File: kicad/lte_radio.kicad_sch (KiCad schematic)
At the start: 24 parts, among them J11 JAE_SIM_Card_SF72S006, J13 Conn_01x06, J14 Conn_01x06, Q1 2N7002, U24 MONARCH_2_GM02S, U26 TXB0108DQSR

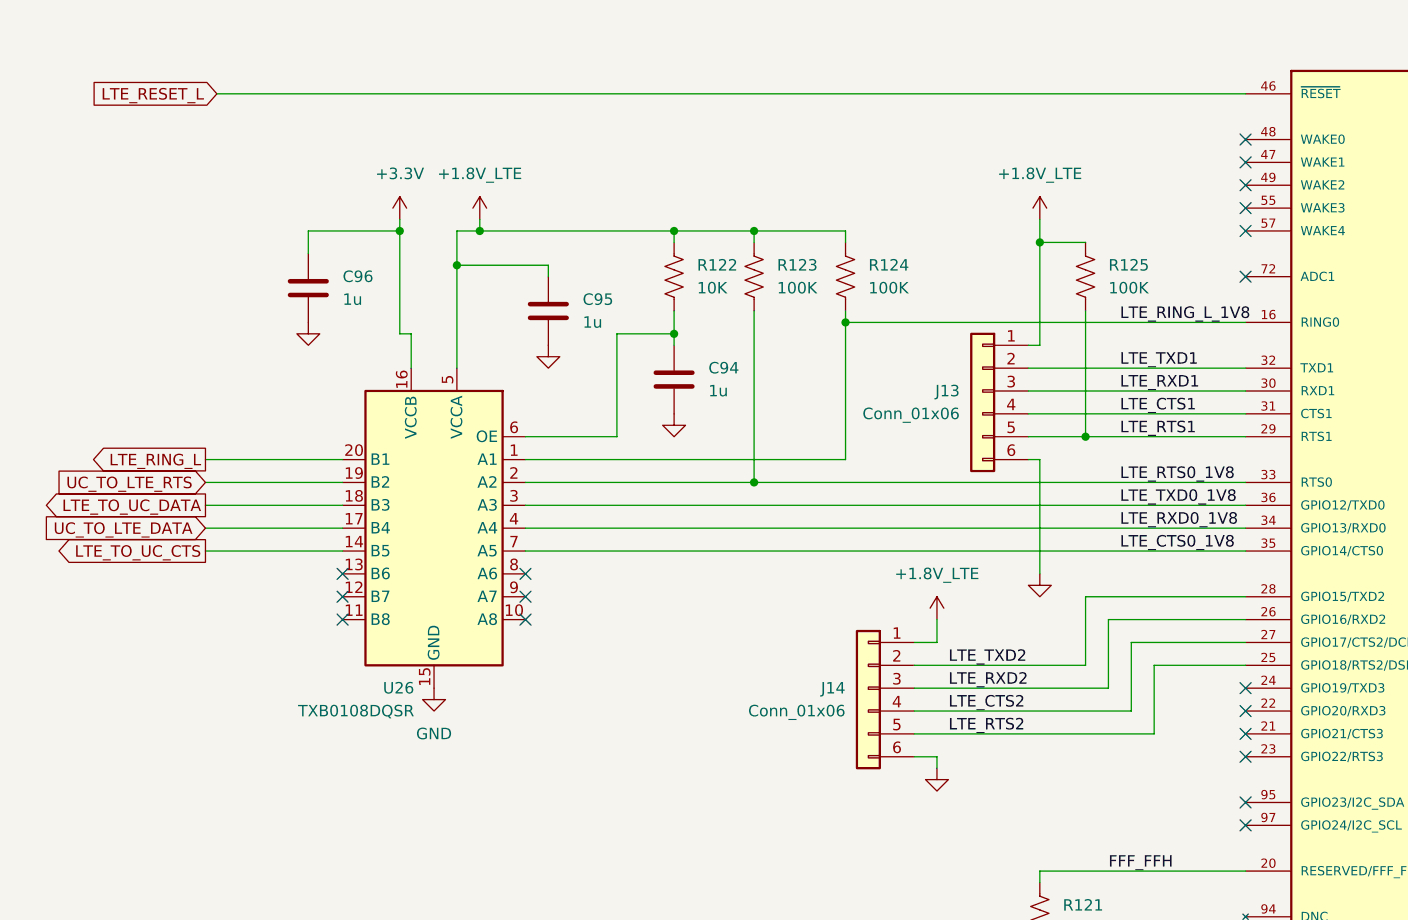
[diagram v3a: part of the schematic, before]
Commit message: swap txb0108 package, fix pin 65 on cpld
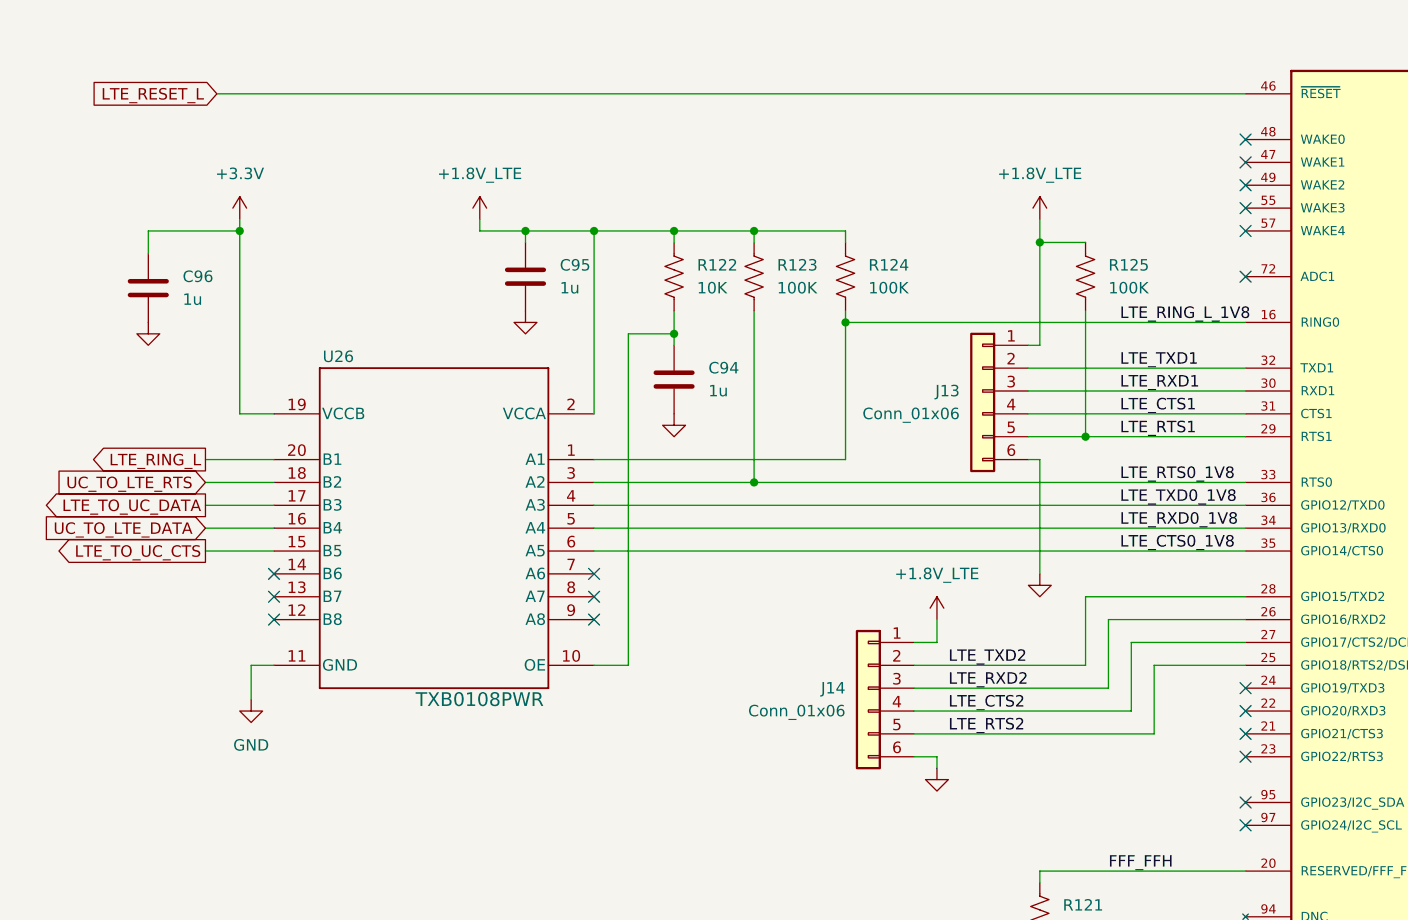
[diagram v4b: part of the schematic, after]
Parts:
- U26: value TXB0108DQSR -> TXB0108PWR; footprint Package_SON:USON-20_2x4mm_P0.4mm -> bgelb_footprint:PW0020A_N; symbol Logic_LevelTranslator:TXB0108DQSR -> bgelb_lib:TXB0108PWR
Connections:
- net +3.3V: now also U26.19 (VCCB), U26.2 (VCCA); no longer U26.16 (VCCB), U26.5 (VCCA)
- net GND: now also U26.11 (GND); no longer U26.15 (GND)
- net LTE_CTS0_1V8: now also U26.6 (A5); no longer U26.7 (A5)
- net LTE_RTS0_1V8: now also U26.3 (A2); no longer U26.2 (A2)
- net LTE_RXD0_1V8: now also U26.5 (A4); no longer U26.4 (A4)
- net LTE_TO_UC_CTS: now also U26.15 (B5); no longer U26.14 (B5)
- net LTE_TO_UC_DATA: now also U26.17 (B3); no longer U26.18 (B3)
- net LTE_TXD0_1V8: now also U26.4 (A3); no longer U26.3 (A3)
- net UC_TO_LTE_DATA: now also U26.16 (B4); no longer U26.17 (B4)
- net UC_TO_LTE_RTS: now also U26.18 (B2); no longer U26.19 (B2)
- net at U26.10 (OE): now also C94.1, R122.2
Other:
- moved on the sheet: C95, C96

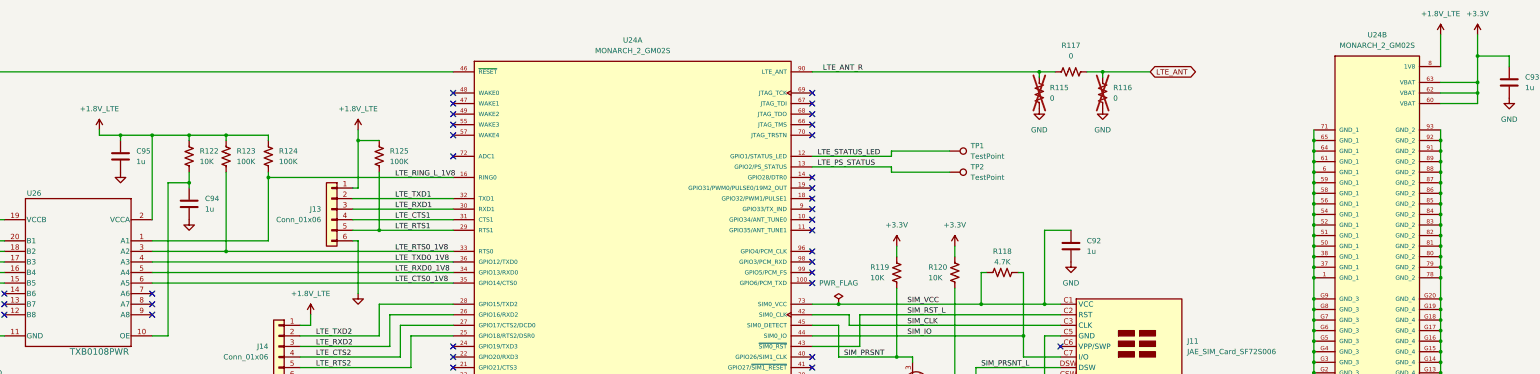
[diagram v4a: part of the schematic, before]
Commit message: kicad version update
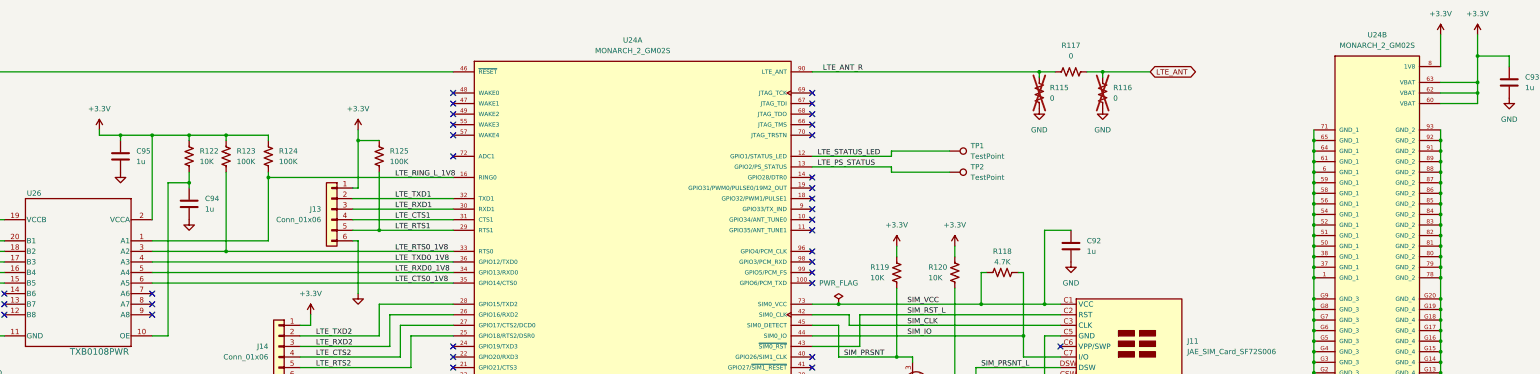
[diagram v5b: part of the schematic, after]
